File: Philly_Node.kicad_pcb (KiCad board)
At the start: 2 copper layers, 22 x 39 mm, 66 parts, among them J1 *, J2 LED, J4 USB_C_Receptacle_USB2.0, J5 Multi, Q1 Q_Dual_NMOS_G1S2G2D2S1D1, Q4 Q_NMOS_GSD, SW2 D0, U1 BQ25176JDSGR, U2 MDBT50Q-U1MV2, U3 E22-900M22S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

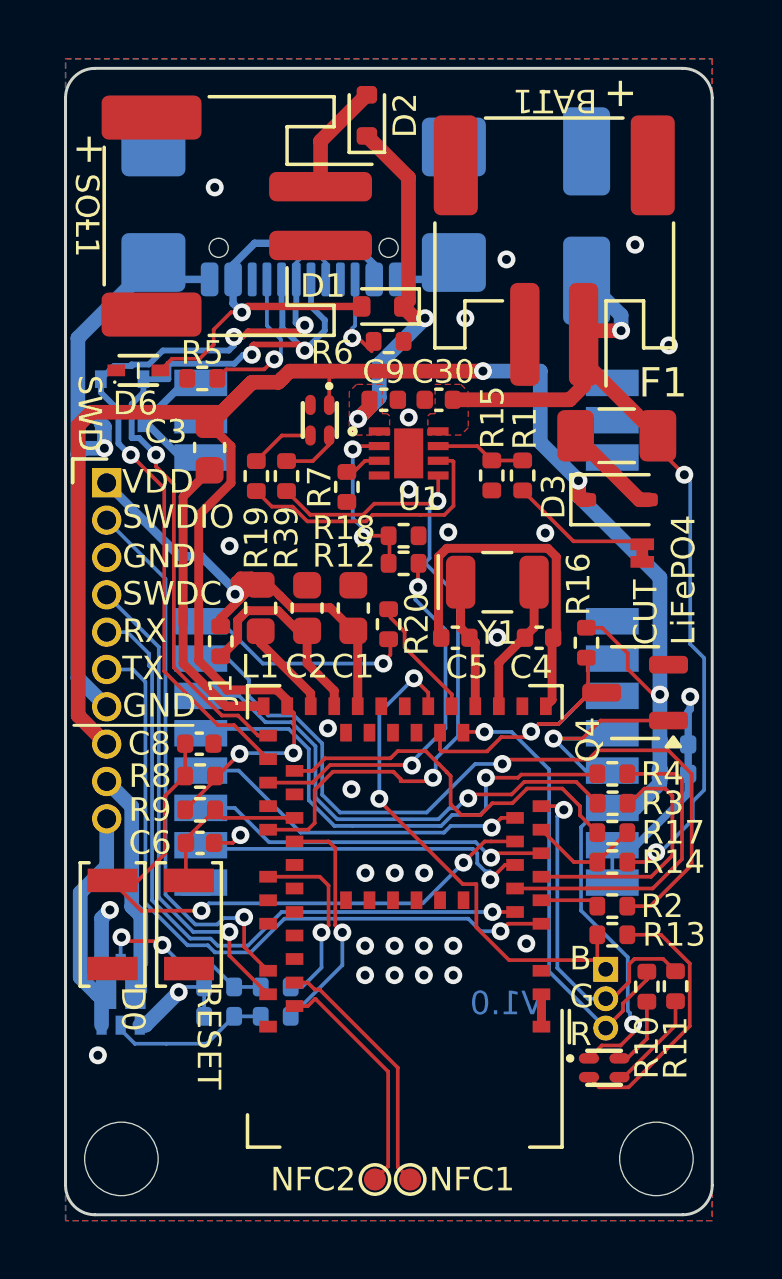
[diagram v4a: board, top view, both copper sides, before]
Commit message: Changes to powerpath, added test points for battery/solar, misc other.
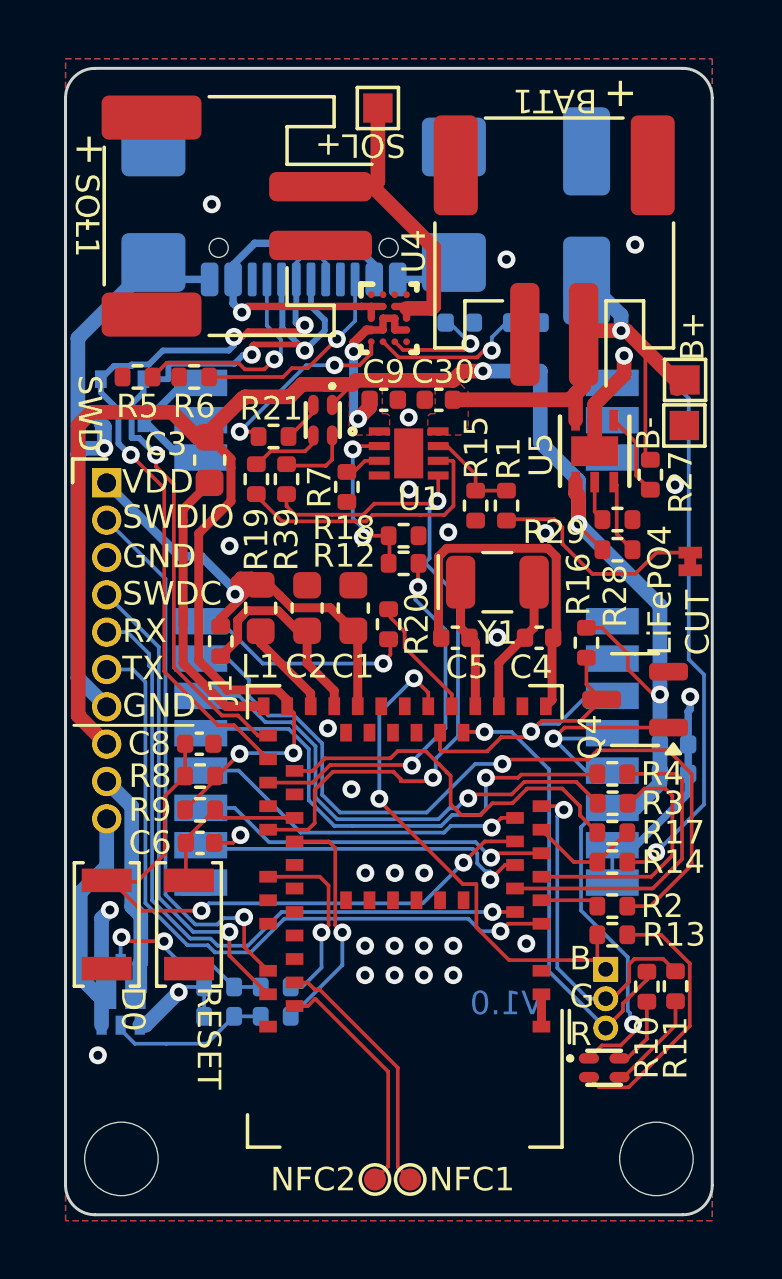
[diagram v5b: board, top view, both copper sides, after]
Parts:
- removed D1, D2: B5819WT, Philly_Lib:D_SOD-523
- removed D3: 1N5819WS, Philly_Lib:D_SOD-323
- removed D6: LESD5D5_0CT1G, Philly_Lib:SOD-523_L1.2-W0.8-LS1.6-BI
- removed F1: Polyfuse 3.5A, Philly_Lib:Fuse_1206_3216Metric
- added C10: 0.1uF, Philly_Lib:C_0402_1005Metric, B.Cu at (93.4, 53.6)
- added R21: 10K, Philly_Lib:R_0402_1005Metric, F.Cu at (87.1, 57.5)
- added R26: 34.8k, Philly_Lib:R_0402_1005Metric, B.Cu at (95.7, 53.6)
- added R27: 300k, Philly_Lib:R_0402_1005Metric, F.Cu at (99.9, 58.8)
- added R28: 300k, Philly_Lib:R_0402_1005Metric, F.Cu at (98.8, 61.4)
- added R29: 34.8k, Philly_Lib:R_0402_1005Metric, F.Cu at (98.8, 60.4)
- added TP1: TestPoint, Philly_Lib:TestPoint_Pad_1.0x1.0mm, F.Cu at (90.6, 46.4)
- added TP2: TestPoint, Philly_Lib:TestPoint_Pad_1.0x1.0mm, F.Cu at (101.0, 57.1)
- added TP3: TestPoint, Philly_Lib:TestPoint_Pad_1.0x1.0mm, F.Cu at (101.1, 55.6)
- added U4: TPS2120YFPR, Philly_Lib:YFP0020AAAA, F.Cu at (91.0, 53.5)
- added U5: TPS25200DRVT, Philly_Node_Lib:DRV6_1X1P6_TEX, F.Cu at (98.0, 58.0)
- moved R6 6.72 mm to (84.4, 55.5), turned to 0 degrees
- moved R5 2.20 mm to (82.5, 55.5)
- moved JP2 1.65 mm to (101.2, 61.8)
- moved R1 1.16 mm to (95.0, 59.9)
- moved R15 1.16 mm to (94.0, 59.9)
- moved C3 0.43 mm to (84.9, 58.3)
- moved Q4 0.24 mm to (99.4, 66.5)
- moved SW2 0.20 mm to (81.4, 74.1)
- moved R19 0.11 mm to (86.5, 59.0)
- moved R39 0.11 mm to (87.5, 59.0)
- moved LED2 0.10 mm to (88.8, 57.0)
- turned C7 to -90 degrees
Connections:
- LED2 pad 4: unconnected-(LED2-B--Pad4) -> Net-(LED2-B-)
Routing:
- net /VBAT_UNFUSED: track 32.3 -> 41.8 mm, vias 3 -> 2
- net /VSOLAR: track 3.78 -> 11.2 mm
- net ST: track 0.00 -> 7.12 mm, vias 0 -> 2
- net Net-(U1-IN): track 12.6 -> 6.25 mm
- net Net-(U4-ILM): track 0.00 -> 5.33 mm, vias 0 -> 1
- net Net-(J4-CC2): track 3.18 -> 7.22 mm
- net Net-(U4-SS): track 0.00 -> 3.92 mm, vias 0 -> 1
- net /VBAT_FUSED: track 3.40 -> 0.00 mm
- net GND: track 71.2 -> 74.5 mm
- net Net-(U5-EN): track 0.00 -> 2.87 mm
- net Net-(JP2-B): track 4.84 -> 7.67 mm
- net /VBUS: track 15.9 -> 13.2 mm
- net Net-(U5-*FAULT): track 0.00 -> 2.65 mm
- net Net-(J4-CC1): track 5.38 -> 7.98 mm
- net Net-(LED2-B-): track 0.00 -> 1.45 mm
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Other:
- board text added: "B+"
- board text added: "B-"
- board text added: "LiFePO4 CUT"
- board text added: "SOL+"
- board text removed: "CUT LiFePO4"

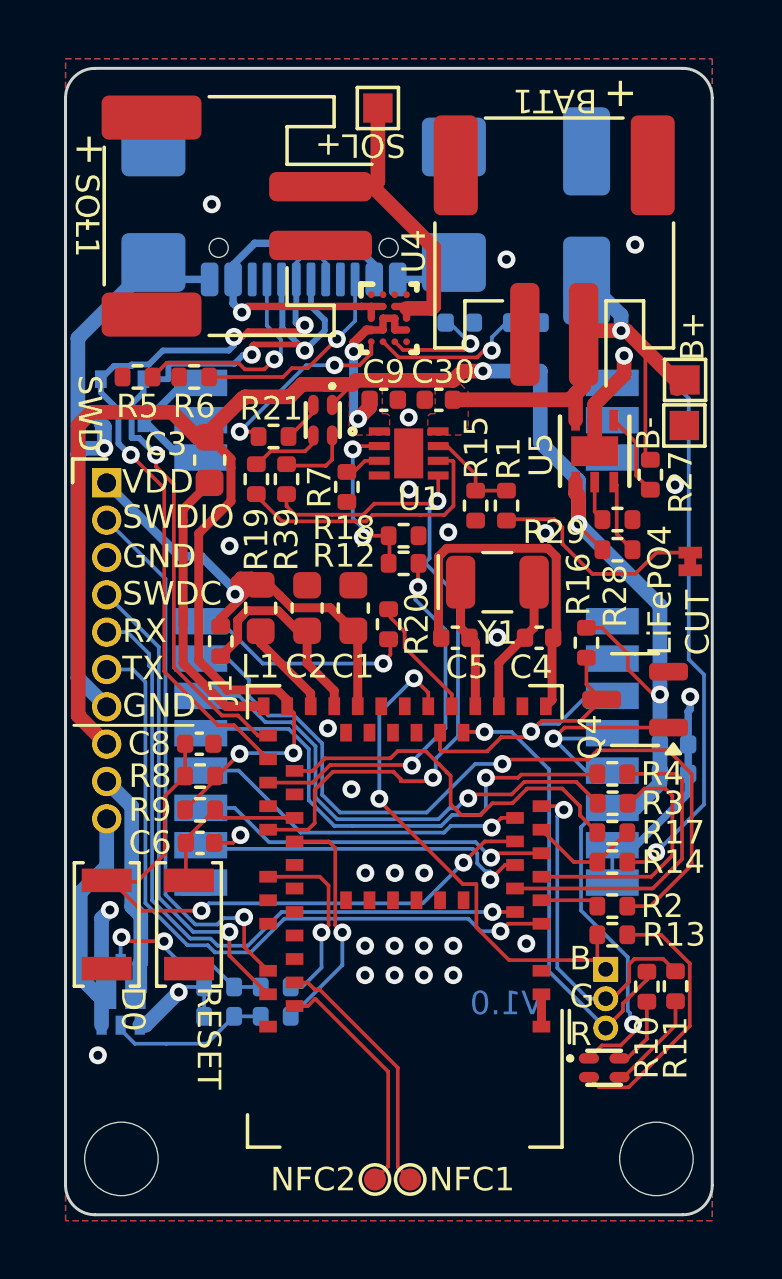
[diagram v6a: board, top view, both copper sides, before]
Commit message: Adjustments to routing, added in more signals for solar input detection.
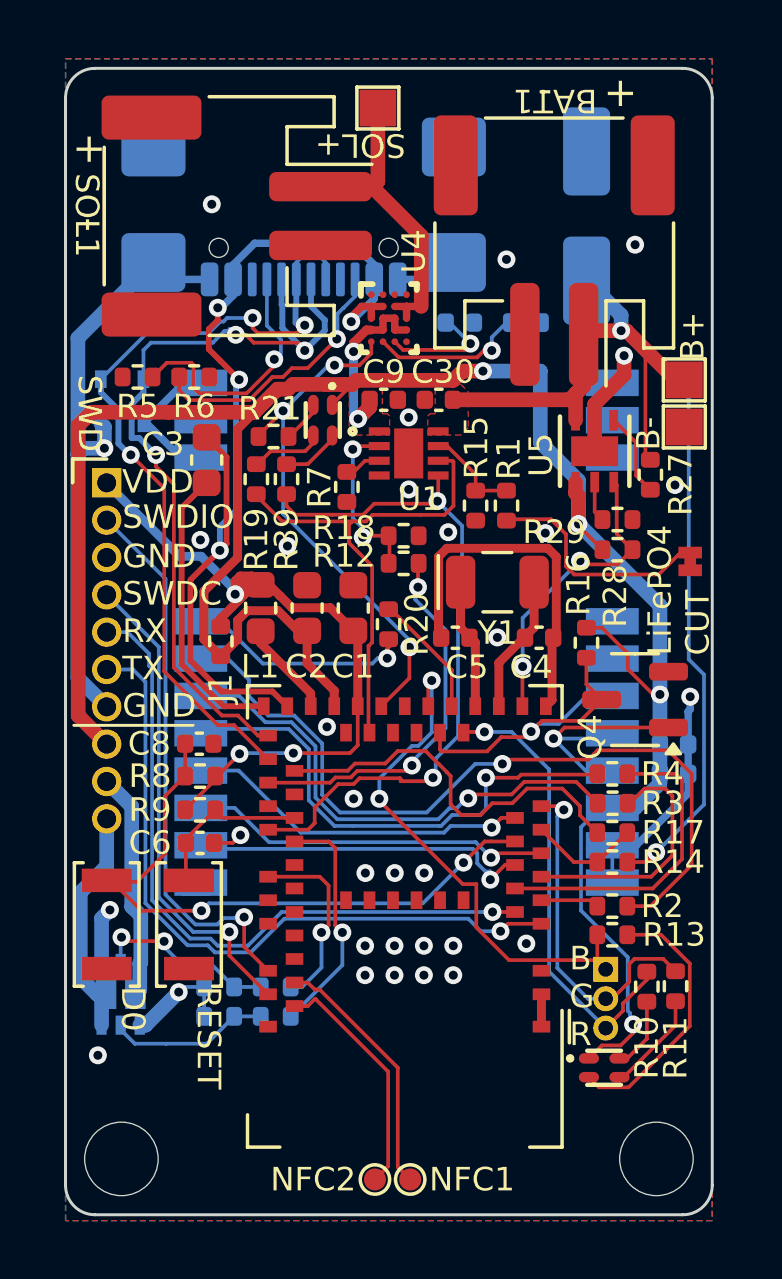
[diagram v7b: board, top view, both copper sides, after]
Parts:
- moved C3 0.10 mm to (84.8, 58.3)
- moved TP2 0.05 mm to (101.0, 57.2)
- turned R6 to 180 degrees
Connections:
- C2 pad 2: Net-(U2-VDDH) -> /VBAT_POL_PROT
- C3 pad 2: /VBAT_POL_PROT -> /VBUS
- J1 pad 2: Net-(U2-VDDH) -> /VBAT_POL_PROT
- R28 pad 2: Net-(U5-*FAULT) -> ~{FLT}
- R8 pad 2: /VBAT_POL_PROT -> /VDD
- R9 pad 2: /VBAT_POL_PROT -> /VDD
- U2 pad 16: unconnected-(U2-P0.27-Pad16) -> ~{FLT}
- U2 pad 26: unconnected-(U2-TRACEDATA3/P1.09-Pad26) -> ST
- U2 pad 27: unconnected-(U2-TRACEDATA2/P0.11-Pad27) -> ~{PG}
- U2 pad 30: Net-(U2-VDDH) -> /VBAT_POL_PROT
- U2 pad 32: /VBAT_POL_PROT -> /VBUS
- U5 pad 3: Net-(U5-*FAULT) -> ~{FLT}
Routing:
- net /VBUS: track 13.2 -> 32.8 mm, vias 1 -> 4
- net ST: track 7.12 -> 17.9 mm, vias 2 -> 3
- net ~{FLT}: track 0.00 -> 10.5 mm, vias 0 -> 2
- net /VDD: track 16.7 -> 24.9 mm, vias 1 -> 3
- net ~{PG}: track 9.32 -> 16.9 mm
- net Net-(U2-VDDH): track 7.49 -> 0.00 mm
- net Net-(U5-*FAULT): track 2.65 -> 0.00 mm
- net /VBAT_POL_PROT: track 83.4 -> 80.8 mm, vias 6 -> 4
- net GND: track 74.5 -> 72.1 mm, vias 31 -> 32
- net Net-(J4-CC2): track 7.22 -> 9.15 mm
- net /VSOLAR: track 11.2 -> 12.4 mm
- net Net-(J4-CC1): track 7.98 -> 9.16 mm
- net P0.17_~{CHG}: track 24.5 -> 23.6 mm
- net /D-: track 27.2 -> 27.8 mm
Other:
- board text added: "PHILLYMESH.NET MICRO NODE V1.0"
- board text removed: "MICRO NODE"
- board text removed: "PHILLYMESH.NET"
- board text removed: "V1.0"

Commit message: Silkscreen and version number bump
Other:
- board text added: "MICRO NODE"
- board text added: "PHILLYMESH.NET"
- board text added: "V2.0"
- board text removed: "PHILLYMESH.NET MICRO NODE V1.0"
